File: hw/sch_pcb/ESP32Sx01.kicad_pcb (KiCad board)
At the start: 2 copper layers, 60.5 x 50.3 mm, 35 parts, among them J1 HEADER_1x03, J2 USBC_USB4105-GF-A, J3 HEADER_1x12, J4 HEADER_1x12, J5 HEADER_1x12, J6 HEADER_1x03, J7 HEADER_2x05, Q1 BC817-25, SW1 434133025816, SW2 434133025816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

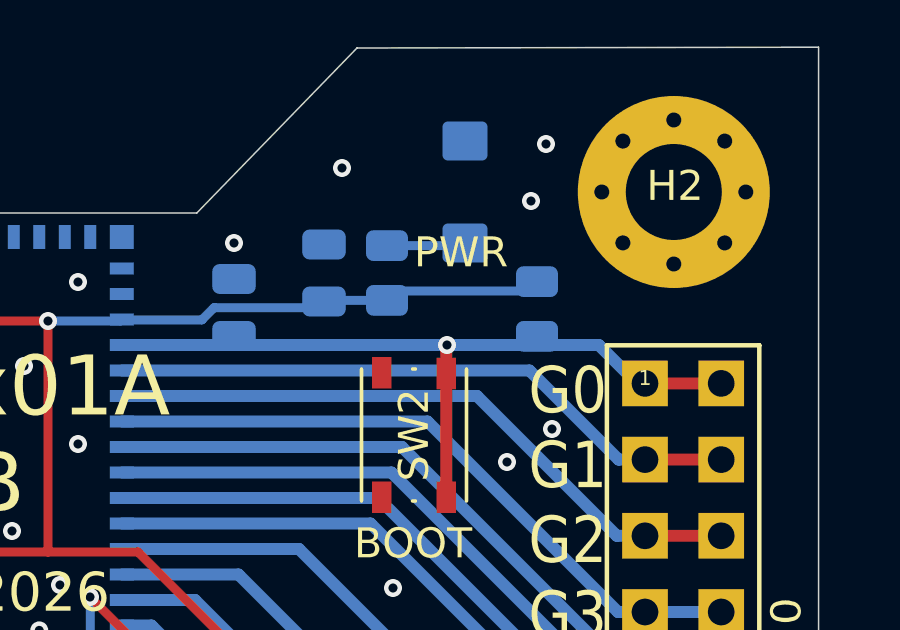
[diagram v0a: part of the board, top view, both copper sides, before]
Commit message: solve missing anotation in schematics
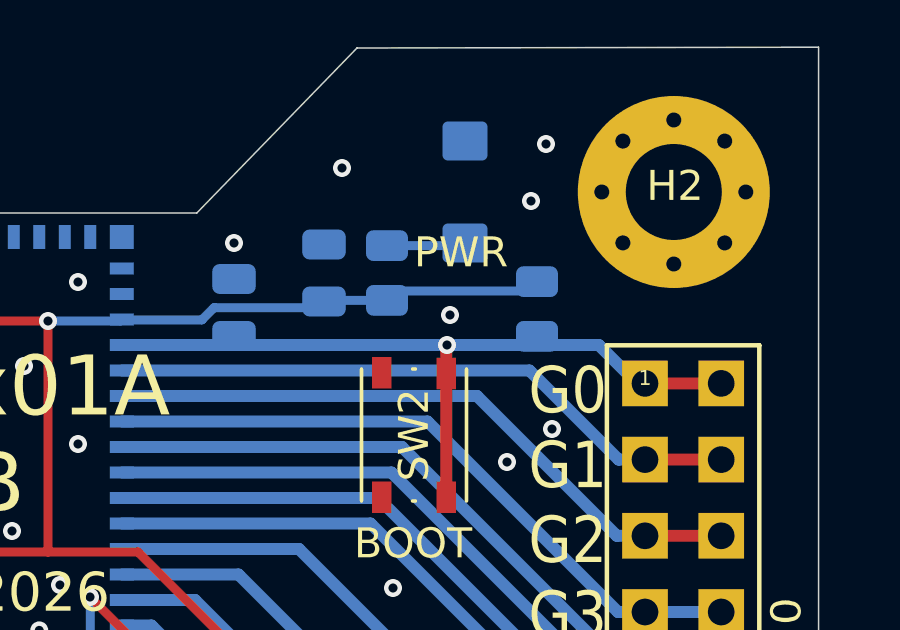
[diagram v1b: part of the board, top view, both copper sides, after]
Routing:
- net GND: vias 51 -> 52
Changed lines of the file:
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@@
+	)
+	(via
+		(at 166.44 88.78)
+		(size 0.6)
+		(drill 0.3)
+		(layers "F.Cu" "B.Cu")
+		(free yes)
+		(net 1)
 	)
 	(via

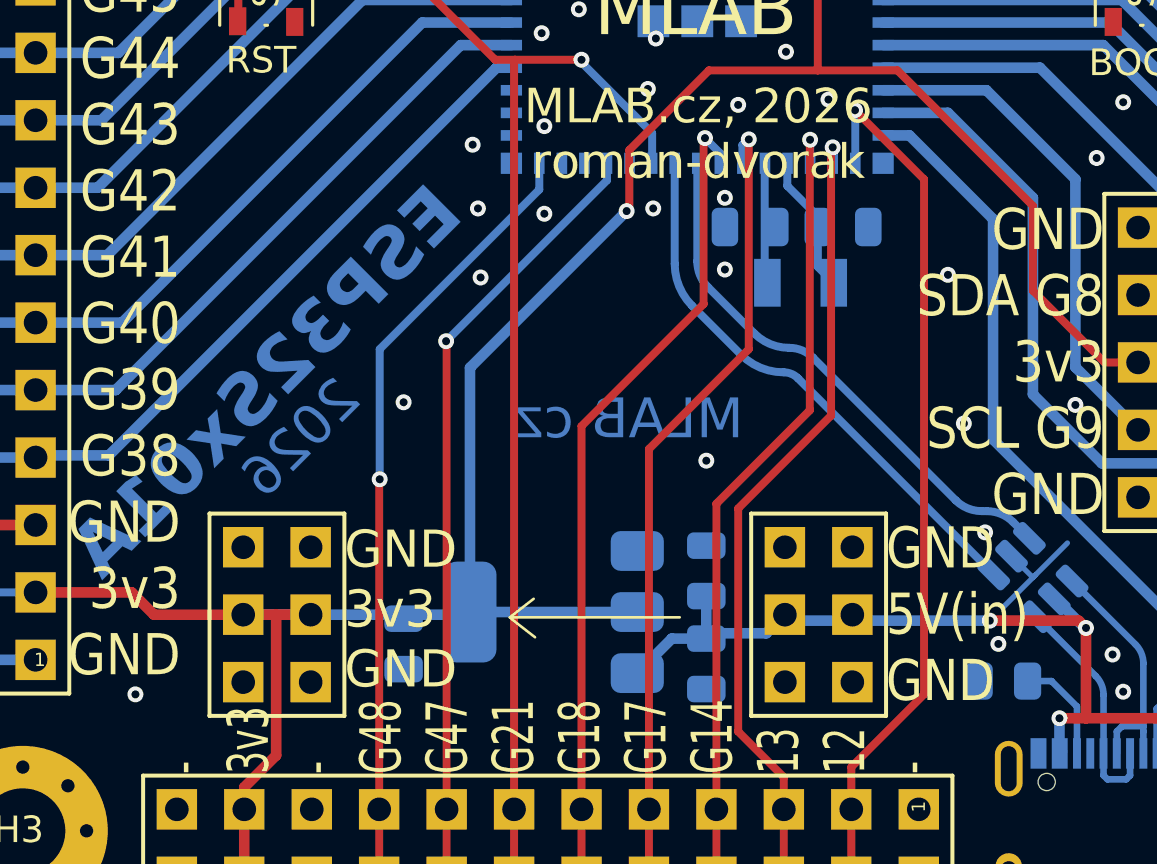
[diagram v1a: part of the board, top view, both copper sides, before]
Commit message: add polarity-swap protection
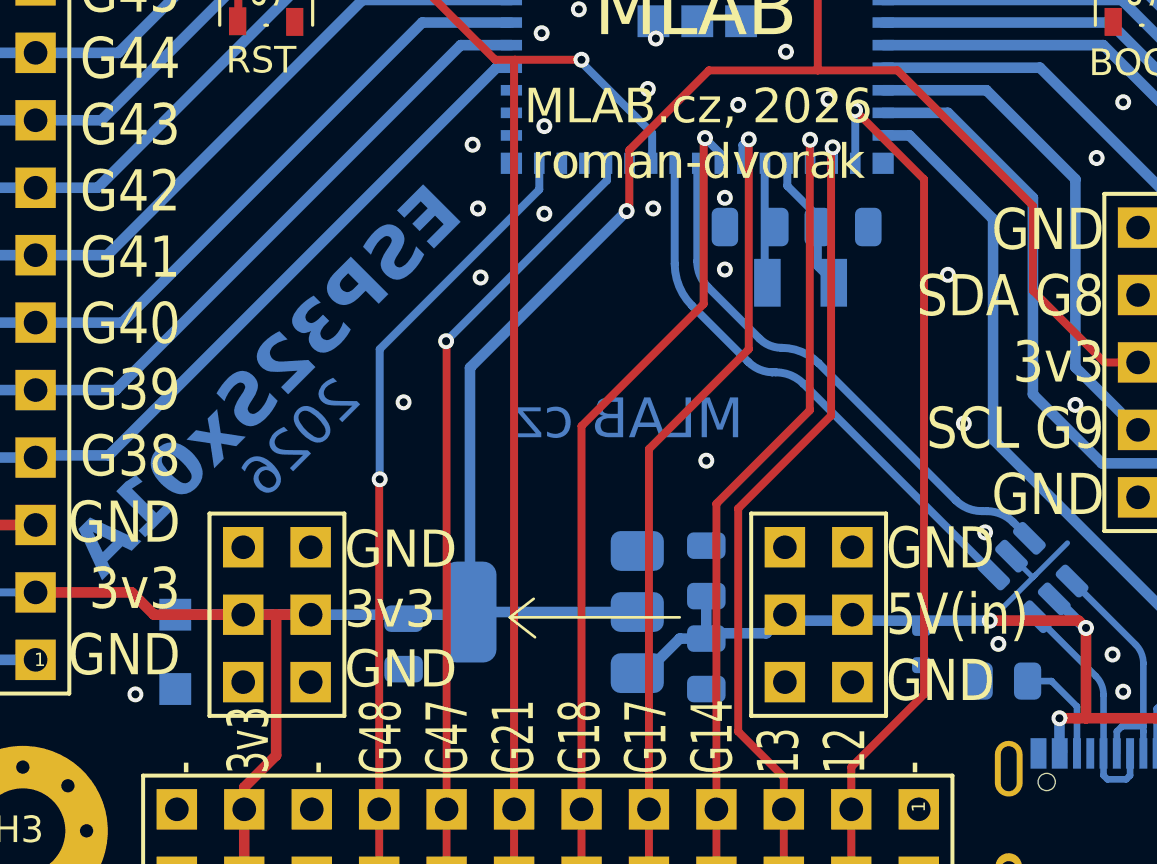
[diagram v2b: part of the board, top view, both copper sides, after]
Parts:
- added D1: BZX585-B5V6.115, Diode_SMD:D_SOD-523, B.Cu at (156.9, 118.4)
- added D2: BZT52H-C3V6,115, Diode_SMD:Nexperia_CFP3_SOD-123W, B.Cu at (128.8, 118.6)
- renumbered D1 to D3, D2 to D4
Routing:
- net +3V3: track 139.5 -> 142.0 mm

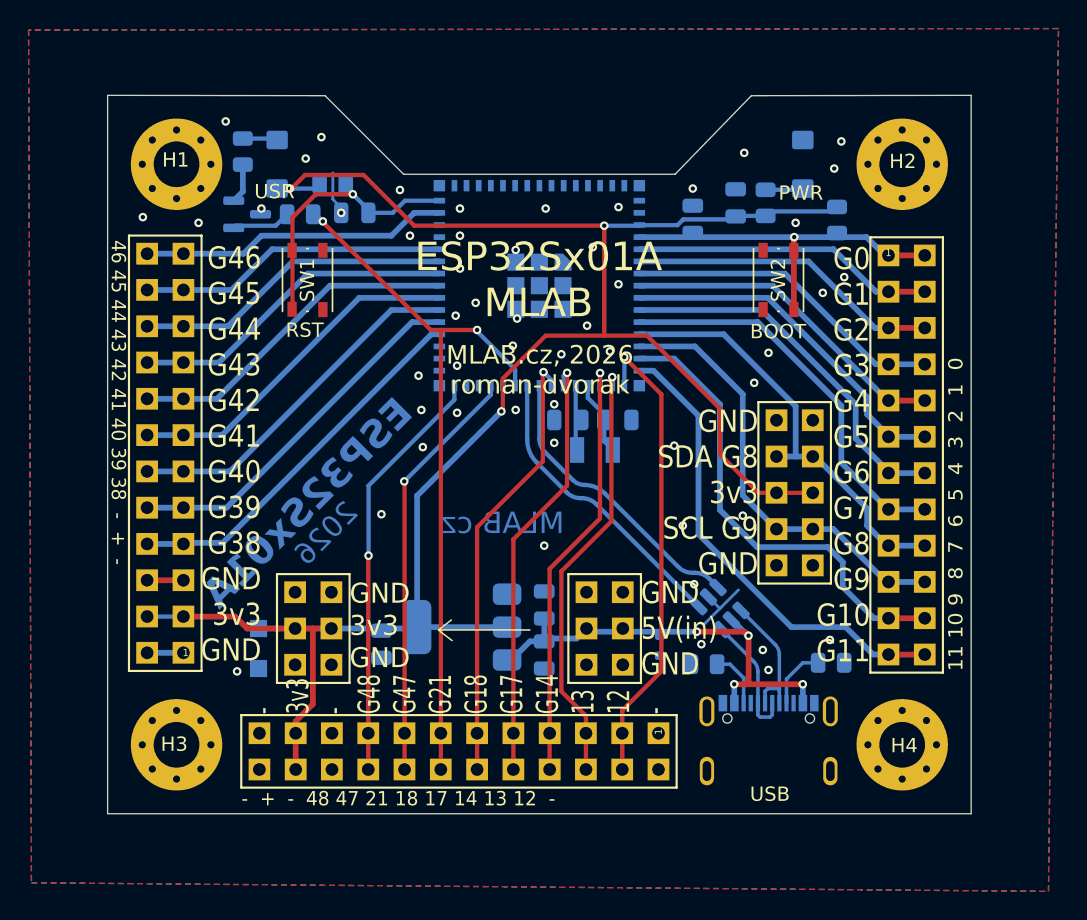
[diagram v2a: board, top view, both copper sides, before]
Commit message: Cleanup fab layer. Resolve DRC errors.
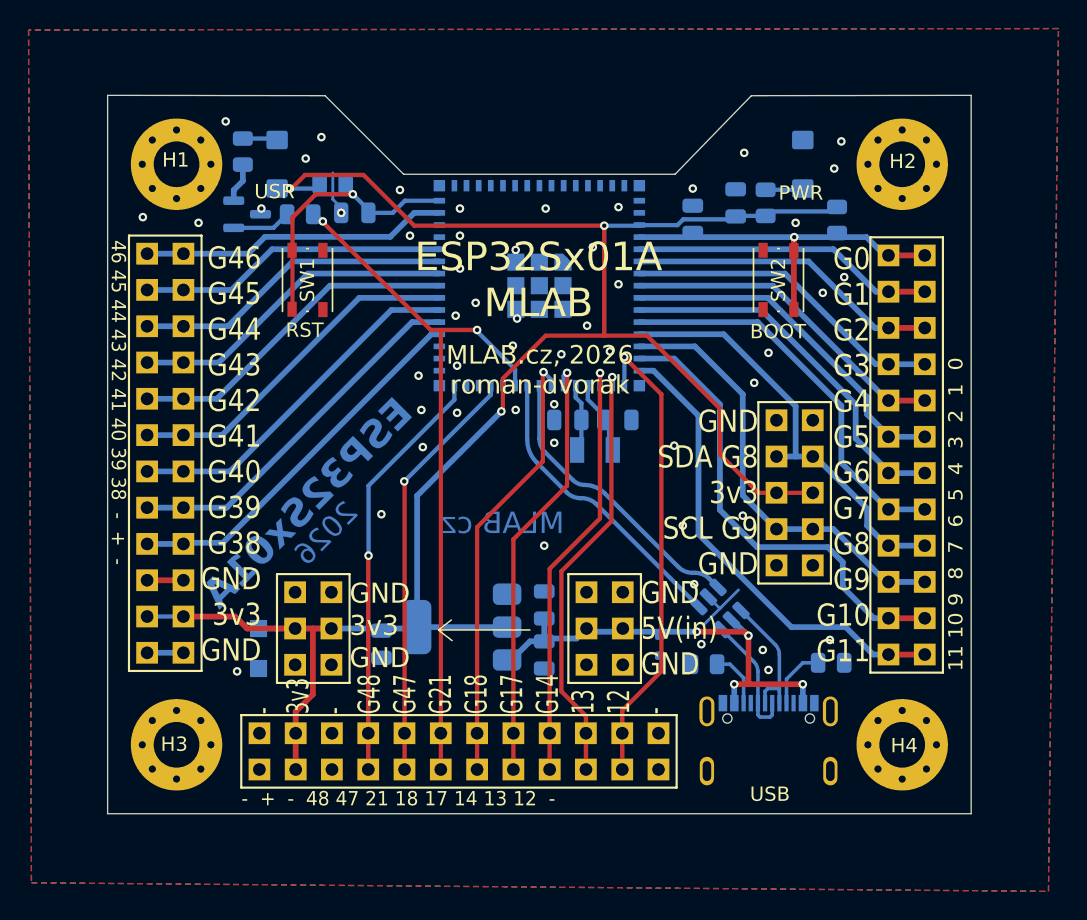
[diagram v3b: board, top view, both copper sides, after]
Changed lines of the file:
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@@
 			(layer "F.SilkS")
 		)
-		(fp_text user "1"
-			(at -1.37 -13.97 90)
-			(layer "F.SilkS")
-			(effects
-				(font
-					(size 0.5 0.5)
-					(thickness 0.05)
-				)
-			)
-		)
 		(pad "1" thru_hole rect
 			(at -1.27 -13.97 270)
@@
 			(layer "F.SilkS")
 		)
-		(fp_text user "1"
-			(at -1.43 -13.97 180)
-			(layer "F.SilkS")
-			(effects
-				(font
-					(size 0.5 0.5)
-					(thickness 0.05)
-				)
-			)
-		)
 		(pad "1" thru_hole rect
 			(at -1.27 -13.97 180)
@@
 			(layer "F.SilkS")
 		)
-		(fp_text user "1"
-			(at -1.27 -14.15 0)
-			(layer "F.SilkS")
-			(effects
-				(font
-					(size 0.5 0.5)
-					(thickness 0.05)
-				)
-			)
-		)
 		(pad "1" thru_hole rect
 			(at -1.27 -13.97)
@@
 		)
 		(property "Value" "200R"
-			(at 0 -1.65 90)
+			(at 3.1674 0.1428 90)
 			(layer "B.Fab")
 			(effects
@@
 		)
 		(fp_text user "${REFERENCE}"
-			(at -1.1875 0.7 90)
+			(at -0.033 0.0158 90)
 			(layer "B.Fab")
 			(effects
@@
 		)
 		(property "Value" "390R"
-			(at 0 -1.65 90)
+			(at -3.3289 0.0172 90)
 			(layer "B.Fab")
 			(effects
@@
 		)
 		(property "Value" "100n"
-			(at 0 -1.679999 0)
+			(at -0.019301 -2.7214 90)
 			(layer "B.Fab")
 			(effects
@@
 		)
 		(property "Value" "200R"
-			(at 0 -1.65 0)
+			(at -0.0597 -2.8754 90)
 			(layer "B.Fab")
 			(effects
@@
 		)
 		(property "Value" "100n"
-			(at 0 -1.679999 90)
+			(at -3.211201 -0.0974 90)
 			(layer "B.Fab")
 			(effects
@@
 					(thickness 0.15)
 				)
-				(justify mirror)
 			)
 		)
@@
 		)
 		(property "Value" "BZT52H-C3V6,115"
-			(at 0 -2.000001 90)
+			(at -9.846199 0.0504 90)
 			(layer "B.Fab")
 			(effects
@@
 		(tags "capacitor")
 		(property "Reference" "C1"
-			(at 2.250001 0 180)
+			(at 2.607001 0.0098 180)
 			(layer "B.SilkS")
 			(effects
@@
 			(at 0 -1.679999 0)
 			(layer "B.Fab")
+			(hide yes)
 			(effects
 				(font
@@
 		(tags "Diode SOD523")
 		(property "Reference" "D1"
-			(at 0 1.3 90)
+			(at -2.458 -0.069 90)
 			(layer "B.SilkS")
 			(effects
@@
 		)
 		(property "Value" "BZX585-B5V6.115"
-			(at 0 -1.399999 90)
+			(at 8.0322 0.0072 90)
 			(layer "B.Fab")
 			(effects
@@
 		)
 		(property "Value" "ESP32-S3-MINI-1"
-			(at 0 -9.4 0)
+			(at 0.4826 0.88 45)
 			(layer "B.Fab")
 			(effects
@@
 		)
 		(fp_text user "${REFERENCE}"
-			(at 0 0 0)
+			(at -4.0894 -3.0062 0)
 			(layer "B.Fab")
 			(effects
@@
 		)
 		(property "Value" "1k"
-			(at 0 0 0)
+			(at 0.0961 -1.527 0)
 			(layer "B.Fab")
 			(effects
@@
 		)
 		(property "Value" "1k"
-			(at 0 -1.65 90)
+			(at 2.1452 0.0628 90)
 			(layer "B.Fab")
 			(effects
@@
 		(tags "resistor")
 		(property "Reference" "R2"
-			(at 2.4875 0 0)
+			(at 2.6629 -1.3728 0)
 			(layer "B.SilkS")
 			(effects
@@
 			(at 0 -1.679999 0)
 			(layer "B.Fab")
+			(hide yes)
 			(effects
 				(font
@@
 		)
 		(property "Value" "BC817-25"
-			(at 0 -2.4 0)
+			(at -4.9908 0.0306 0)
 			(layer "B.Fab")
 			(effects
@@
 		)
 		(property "Value" "10u"
-			(at 0 -1.679999 90)
+			(at -2.5832 -0.1002 90)
 			(layer "B.Fab")
 			(effects
@@
 		(tags "SOT TO_SOT_SMD")
 		(property "Reference" "U2"
-			(at 0 2.4 135)
+			(at -1.1144 -2.384647 135)
 			(layer "B.SilkS")
 			(effects
@@
 					(thickness 0.15)
 				)
-				(justify mirror)
 			)
 		)
@@
 	)
 	(segment
-		(start 131.44 123.68)
-		(end 131.44 124.51)
-		(width 0.4)
-		(layer "F.Cu")
-		(net 3)
-	)
-	(segment
 		(start 131.399998 117.18)
 		(end 128.04 117.18)
@@
 	)
 	(segment
+		(start 131.44 122.9998)
+		(end 131.44 124.51)
+		(width 0.4)
+		(layer "F.Cu")
+		(net 3)
+	)
+	(segment
 		(start 161.14 101.78)
 		(end 161.14 104.98)
@@
 	)
 	(segment
+		(start 132.64 121.7998)
+		(end 131.44 122.9998)
+		(width 0.4)
+		(layer "F.Cu")
+		(net 3)
+	)
+	(segment
 		(start 153.04 88.98)
 		(end 153.04 96.68)
@@
 	)
 	(segment
-		(start 127.2 116.34)
-		(end 123.58 116.34)
+		(start 132.64 117.18)
+		(end 132.64 121.7998)
 		(width 0.4)
 		(layer "F.Cu")
@@
 	)
 	(segment
-		(start 132.64 117.18)
-		(end 132.64 122.48)
+		(start 127.2 116.34)
+		(end 123.58 116.34)
 		(width 0.4)
 		(layer "F.Cu")
@@
 	)
 	(segment
-		(start 132.64 122.48)
-		(end 131.44 123.68)
-		(width 0.4)
-		(layer "F.Cu")
-		(net 3)
-	)
-	(segment
 		(start 148.94 96.68)
 		(end 153.04 96.68)
@@
 	(segment
 		(start 127.74 84.705)
-		(end 127.74 86.5925)
+		(end 127.74 85.8566)
 		(width 0.4)
 		(layer "B.Cu")
@@
 	)
 	(segment
-		(start 127.74 86.5925)
+		(start 127.1025 86.4941)
 		(end 127.1025 87.23)
 		(width 0.4)
@@
 	)
 	(segment
-		(start 127.164999 89.067501)
-		(end 127.1025 89.13)
-		(width 0.3)
+		(start 127.74 85.8566)
+		(end 127.1025 86.4941)
+		(width 0.4)
 		(layer "B.Cu")
-		(net 13)
+		(net 12)
 	)
 	(segment
-		(start 130.04 88.98)
-		(end 130.84 88.18)
+		(start 127.164999 89.067501)
+		(end 127.1025 89.13)
 		(width 0.3)
 		(layer "B.Cu")
@@
 	(segment
 		(start 127.1025 89.13)
-		(end 127.2525 88.98)
+		(end 129.89 89.13)
 		(width 0.3)
 		(layer "B.Cu")
@@
 	)
 	(segment
-		(start 127.2525 88.98)
-		(end 130.04 88.98)
+		(start 129.89 89.13)
+		(end 130.84 88.18)
 		(width 0.3)
 		(layer "B.Cu")
@@
 	)
 	(segment
-		(start 151.890001 100.18)
-		(end 151.890001 101.030001)
+		(start 151.890001 101.151001)
+		(end 153.04 102.301)
 		(width 0.3)
 		(layer "B.Cu")
@@
 	)
 	(segment
-		(start 153.04 102.18)
-		(end 153.04 104.08)
+		(start 153.3768 102.9168)
+		(end 153.3768 104.4168)
 		(width 0.3)
 		(layer "B.Cu")
@@
 	)
 	(segment
-		(start 153.04 104.08)
+		(start 153.3768 104.4168)
 		(end 153.64 104.68)
 		(width 0.3)
@@
 	)
 	(segment
-		(start 151.890001 101.030001)
-		(end 153.04 102.18)
+		(start 153.04 102.58)
+		(end 153.3768 102.9168)
+		(width 0.3)
+		(layer "B.Cu")
+		(net 17)
+	)
+	(segment
+		(start 153.04 102.301)
+		(end 153.04 102.58)
+		(width 0.3)
+		(layer "B.Cu")
+		(net 17)
+	)
+	(segment
+		(start 151.890001 100.18)
+		(end 151.890001 101.151001)
 		(width 0.3)
 		(layer "B.Cu")
@@
 	)
 	(segment
-		(start 129.04 89.68)
-		(end 127.78 90.94)
+		(start 138.06 89.76)
+		(end 129.2976 89.76)
 		(width 0.4)
 		(layer "B.Cu")
@@
 	)
 	(segment
-		(start 127.78 90.94)
-		(end 121.04 90.94)
+		(start 139.74 88.08)
+		(end 138.06 89.76)
 		(width 0.4)
 		(layer "B.Cu")
@@
 	)
 	(segment
-		(start 138.14 89.68)
-		(end 129.04 89.68)
+		(start 141.5 88.08)
+		(end 139.74 88.08)
 		(width 0.4)
 		(layer "B.Cu")
@@
 	)
 	(segment
-		(start 141.5 88.08)
-		(end 139.74 88.08)
+		(start 129.2976 89.76)
+		(end 128.1176 90.94)
 		(width 0.4)
 		(layer "B.Cu")
@@
 	)
 	(segment
-		(start 139.74 88.08)
-		(end 138.14 89.68)
+		(start 128.1176 90.94)
+		(end 121.04 90.94)
 		(width 0.4)
 		(layer "B.Cu")
@@
 	)
 	(segment
-		(start 151.04 104.58)
-		(end 151.14 104.68)
+		(start 151.44 101.40952)
+		(end 151.44 104.38)
 		(width 0.3)
 		(layer "B.Cu")
@@
 	(segment
 		(start 151.04 100.18)
-		(end 151.04 104.58)
+		(end 151.04 101.00952)
+		(width 0.3)
+		(layer "B.Cu")
+		(net 38)
+	)
+	(segment
+		(start 151.44 104.38)
+		(end 151.14 104.68)
+		(width 0.3)
+		(layer "B.Cu")
+		(net 38)
+	)
+	(segment
+		(start 151.04 101.00952)
+		(end 151.44 101.40952)
 		(width 0.3)
 		(layer "B.Cu")
